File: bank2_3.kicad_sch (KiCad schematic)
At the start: 1 part, among them IC1 ECP5-BGA256

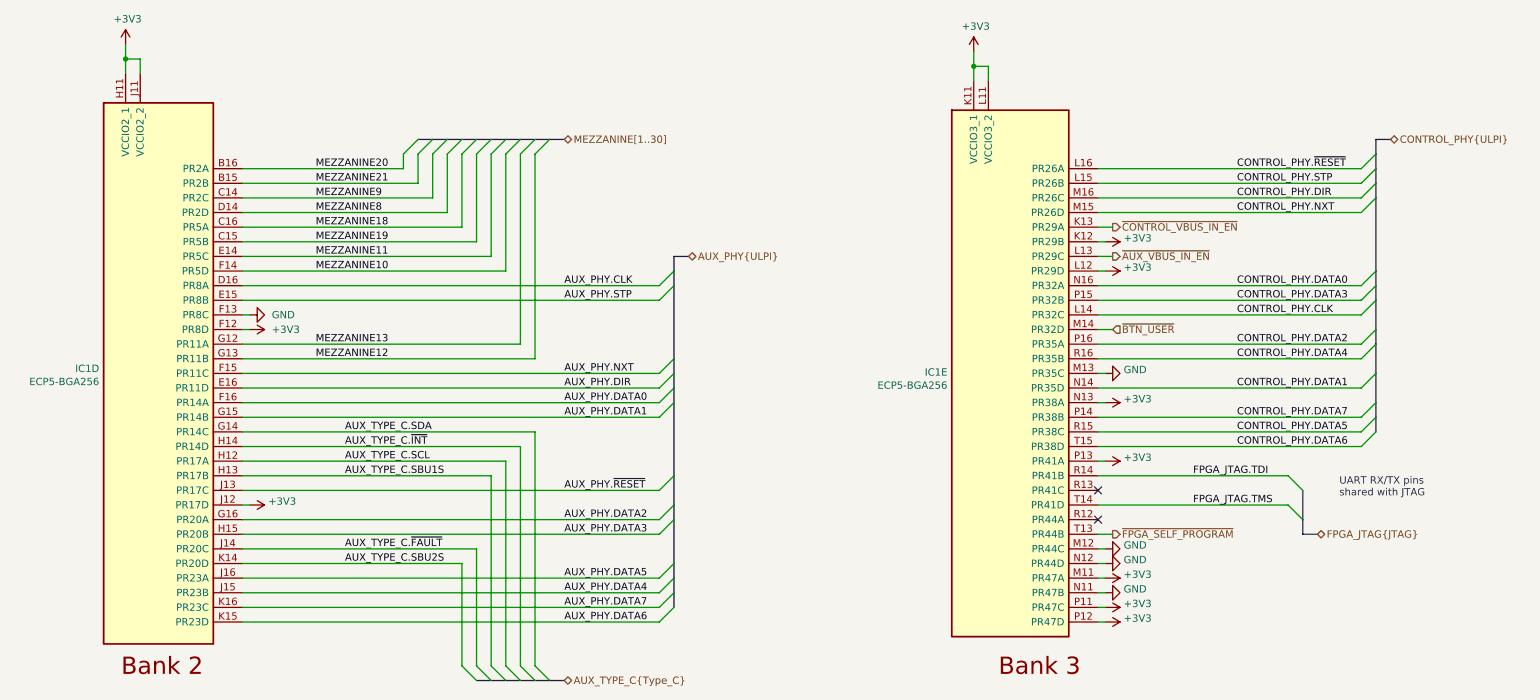
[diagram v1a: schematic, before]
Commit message: Clean up schematic
- Renumber Pmod signal names to match silkscreen labels
- Clean up FPGA symbol
- Clean up PHY symbol
- Add title block to newer sheets
- Fix horizontal line in LED sheet
- Improve various label positions
- Update data sheet fields
- Renumber pages
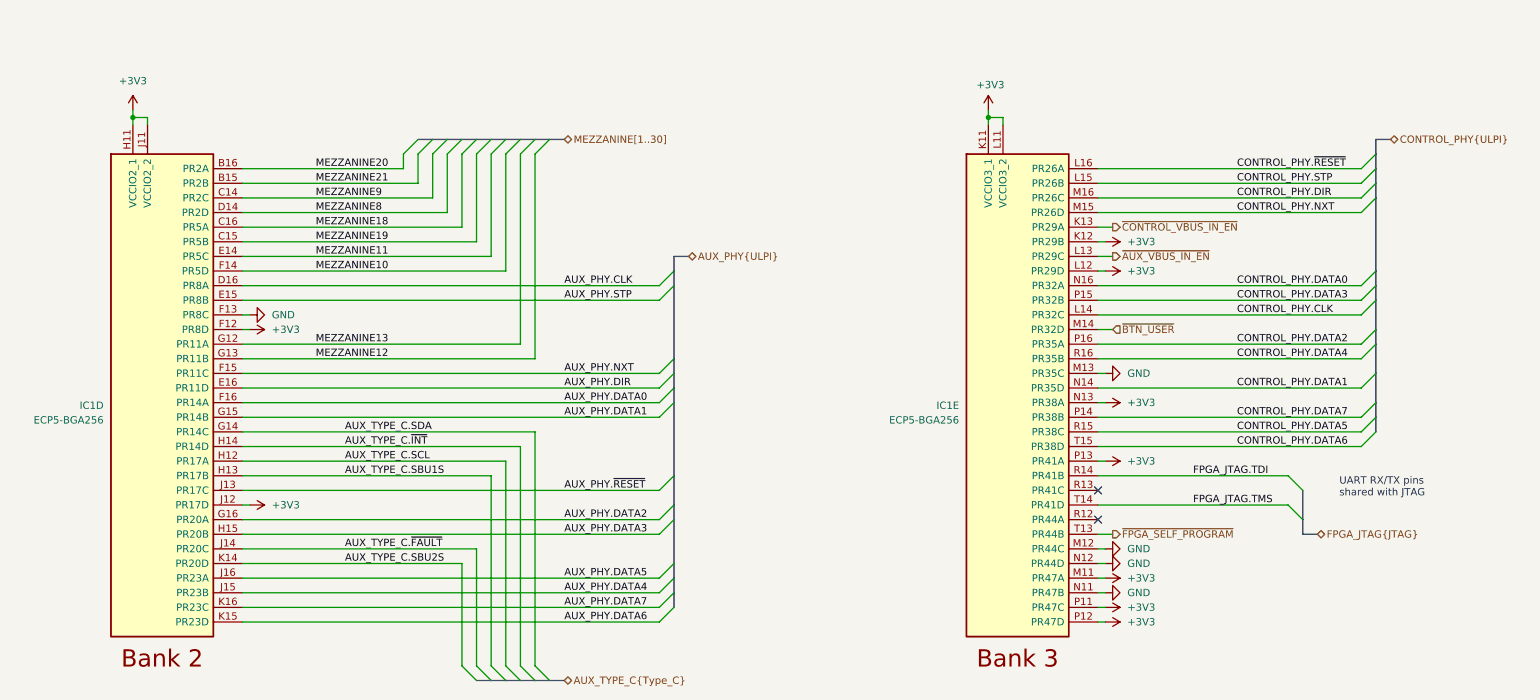
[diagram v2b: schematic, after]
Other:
- moved on the sheet: IC1D, IC1E

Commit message: Update copyright notices
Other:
- company: Copyright 2019-2023 Great Scott Gadgets -> ${COPYRIGHT}
- title: Cynthion -> ${TITLE}
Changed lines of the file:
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@@
   (paper "A4")
   (title_block
-    (title "Cynthion")
+    (title "${TITLE}")
     (date "${DATE}")
     (rev "${VERSION}")
-    (company "Copyright 2019-2023 Great Scott Gadgets")
-    (comment 1 "Licensed under the CERN-OHL-P v2")
+    (company "${COPYRIGHT}")
+    (comment 1 "${LICENSE}")
   )
   (junction (at 38.1 54.61) (diameter 0) (color 0 0 0 0)
